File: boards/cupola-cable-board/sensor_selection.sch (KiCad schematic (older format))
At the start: 6 parts

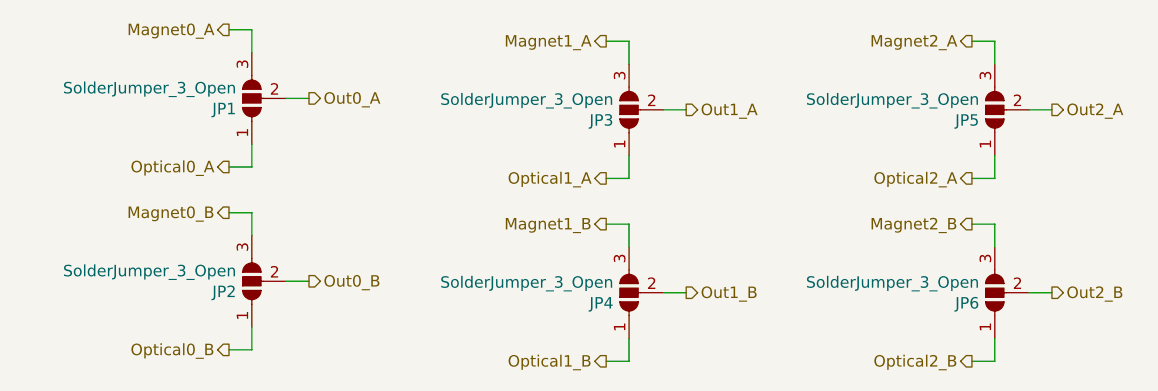
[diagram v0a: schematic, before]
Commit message: cupola_cable_board: 500mA 3.3V regulator, 4 pin connector for magnetic encoder
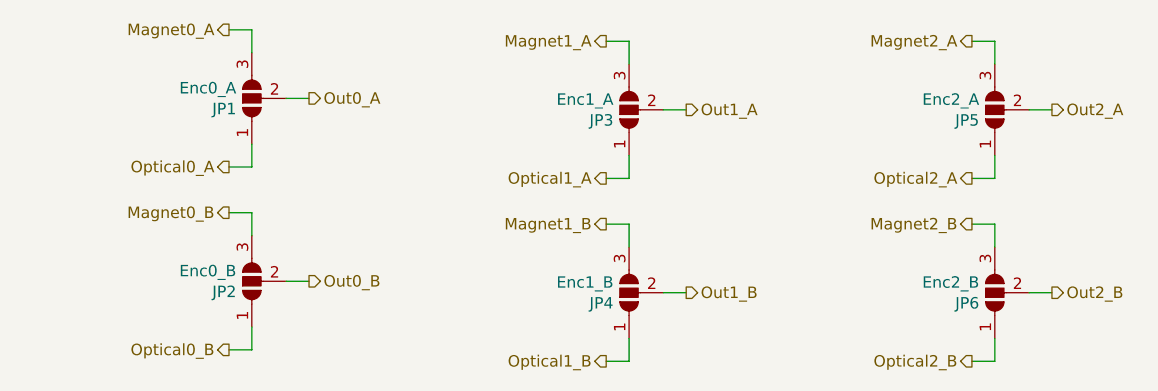
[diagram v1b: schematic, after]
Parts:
- JP1: value SolderJumper_3_Open -> Enc0_A
- JP2: value SolderJumper_3_Open -> Enc0_B
- JP3: value SolderJumper_3_Open -> Enc1_A
- JP4: value SolderJumper_3_Open -> Enc1_B
- JP5: value SolderJumper_3_Open -> Enc2_A
- JP6: value SolderJumper_3_Open -> Enc2_B
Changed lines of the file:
@@
 P 1650 1050
 F 0 "JP1" V 1604 1118 50  0000 L CNN
-F 1 "SolderJumper_3_Open" V 1695 1118 50  0000 L CNN
+F 1 "Enc0_A" V 1695 1118 50  0000 L CNN
 F 2 "" H 1650 1050 50  0001 C CNN
 F 3 "~" H 1650 1050 50  0001 C CNN
@@
 P 3300 1100
 F 0 "JP3" V 3254 1168 50  0000 L CNN
-F 1 "SolderJumper_3_Open" V 3345 1168 50  0000 L CNN
+F 1 "Enc1_A" V 3345 1168 50  0000 L CNN
 F 2 "" H 3300 1100 50  0001 C CNN
 F 3 "~" H 3300 1100 50  0001 C CNN
@@
 P 4900 1100
 F 0 "JP5" V 4854 1168 50  0000 L CNN
-F 1 "SolderJumper_3_Open" V 4945 1168 50  0000 L CNN
+F 1 "Enc2_A" V 4945 1168 50  0000 L CNN
 F 2 "" H 4900 1100 50  0001 C CNN
 F 3 "~" H 4900 1100 50  0001 C CNN
@@
 P 1650 1850
 F 0 "JP2" V 1604 1918 50  0000 L CNN
-F 1 "SolderJumper_3_Open" V 1695 1918 50  0000 L CNN
+F 1 "Enc0_B" V 1695 1918 50  0000 L CNN
 F 2 "" H 1650 1850 50  0001 C CNN
 F 3 "~" H 1650 1850 50  0001 C CNN
@@
 P 3300 1900
 F 0 "JP4" V 3254 1968 50  0000 L CNN
-F 1 "SolderJumper_3_Open" V 3345 1968 50  0000 L CNN
+F 1 "Enc1_B" V 3345 1968 50  0000 L CNN
 F 2 "" H 3300 1900 50  0001 C CNN
 F 3 "~" H 3300 1900 50  0001 C CNN
@@
 P 4900 1900
 F 0 "JP6" V 4854 1968 50  0000 L CNN
-F 1 "SolderJumper_3_Open" V 4945 1968 50  0000 L CNN
+F 1 "Enc2_B" V 4945 1968 50  0000 L CNN
 F 2 "" H 4900 1900 50  0001 C CNN
 F 3 "~" H 4900 1900 50  0001 C CNN

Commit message: cupola board: footprints for solder jumpers
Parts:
- JP1, JP2, JP3, JP4, JP5, JP6: footprint (none) -> Jumper:SolderJumper-3_P1.3mm_Open_RoundedPad1.0x1.5mm
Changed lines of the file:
@@
 F 0 "JP1" V 1604 1118 50  0000 L CNN
 F 1 "Enc0_A" V 1695 1118 50  0000 L CNN
-F 2 "" H 1650 1050 50  0001 C CNN
+F 2 "Jumper:SolderJumper-3_P1.3mm_Open_RoundedPad1.0x1.5mm" H 1650 1050 50  0001 C CNN
 F 3 "~" H 1650 1050 50  0001 C CNN
 	1    1650 1050
@@
 F 0 "JP3" V 3254 1168 50  0000 L CNN
 F 1 "Enc1_A" V 3345 1168 50  0000 L CNN
-F 2 "" H 3300 1100 50  0001 C CNN
+F 2 "Jumper:SolderJumper-3_P1.3mm_Open_RoundedPad1.0x1.5mm" H 3300 1100 50  0001 C CNN
 F 3 "~" H 3300 1100 50  0001 C CNN
 	1    3300 1100
@@
 F 0 "JP5" V 4854 1168 50  0000 L CNN
 F 1 "Enc2_A" V 4945 1168 50  0000 L CNN
-F 2 "" H 4900 1100 50  0001 C CNN
+F 2 "Jumper:SolderJumper-3_P1.3mm_Open_RoundedPad1.0x1.5mm" H 4900 1100 50  0001 C CNN
 F 3 "~" H 4900 1100 50  0001 C CNN
 	1    4900 1100
@@
 F 0 "JP2" V 1604 1918 50  0000 L CNN
 F 1 "Enc0_B" V 1695 1918 50  0000 L CNN
-F 2 "" H 1650 1850 50  0001 C CNN
+F 2 "Jumper:SolderJumper-3_P1.3mm_Open_RoundedPad1.0x1.5mm" H 1650 1850 50  0001 C CNN
 F 3 "~" H 1650 1850 50  0001 C CNN
 	1    1650 1850
@@
 F 0 "JP4" V 3254 1968 50  0000 L CNN
 F 1 "Enc1_B" V 3345 1968 50  0000 L CNN
-F 2 "" H 3300 1900 50  0001 C CNN
+F 2 "Jumper:SolderJumper-3_P1.3mm_Open_RoundedPad1.0x1.5mm" H 3300 1900 50  0001 C CNN
 F 3 "~" H 3300 1900 50  0001 C CNN
 	1    3300 1900
@@
 F 0 "JP6" V 4854 1968 50  0000 L CNN
 F 1 "Enc2_B" V 4945 1968 50  0000 L CNN
-F 2 "" H 4900 1900 50  0001 C CNN
+F 2 "Jumper:SolderJumper-3_P1.3mm_Open_RoundedPad1.0x1.5mm" H 4900 1900 50  0001 C CNN
 F 3 "~" H 4900 1900 50  0001 C CNN
 	1    4900 1900
